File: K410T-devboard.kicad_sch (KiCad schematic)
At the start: 0 parts

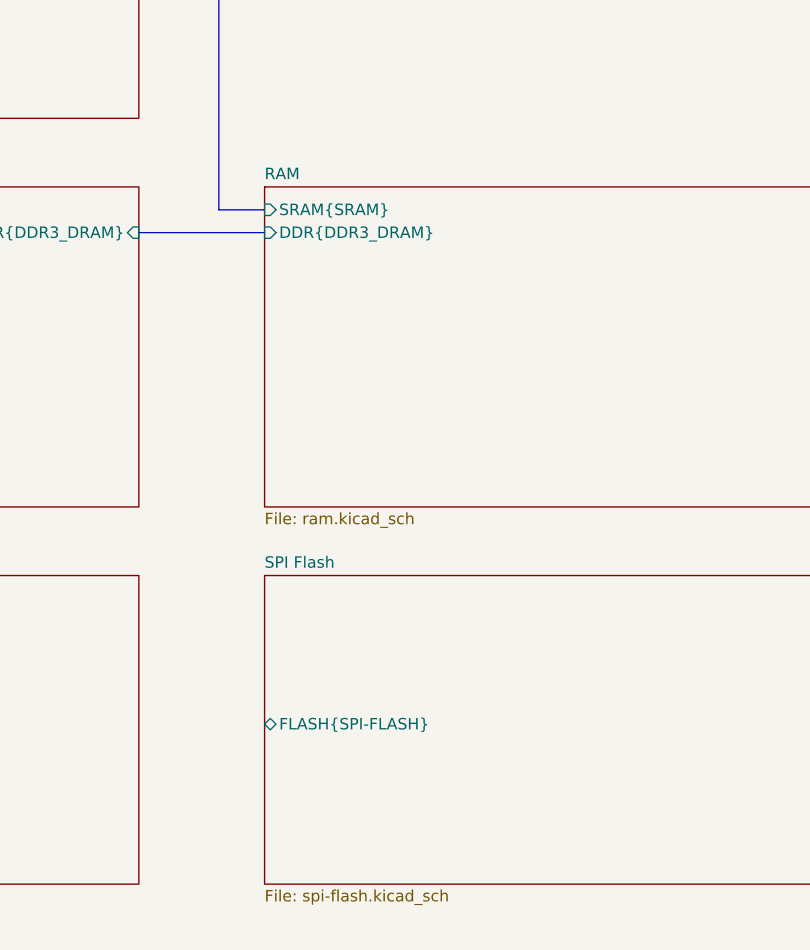
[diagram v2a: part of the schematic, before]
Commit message: Add SD-CARD bus. Add user SPI flash, rename main SPI flash bus. Add uSD card slot
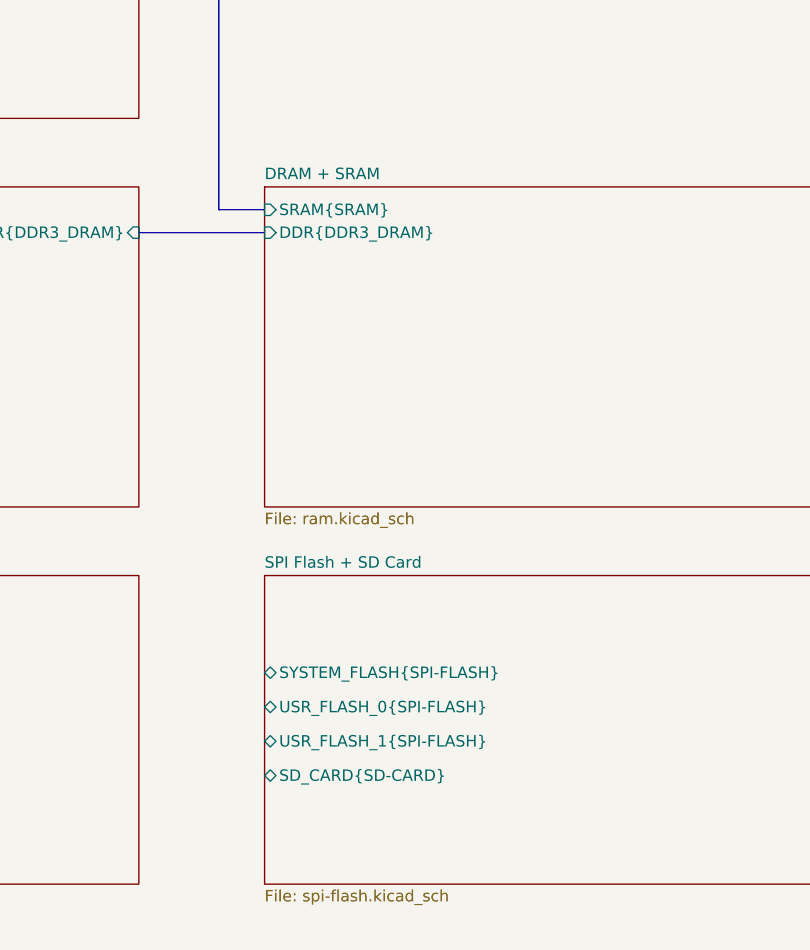
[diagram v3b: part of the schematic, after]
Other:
- sheet RAM renamed DRAM + SRAM
- sheet SPI Flash renamed SPI Flash + SD Card
- sheet SPI Flash + SD Card ports: added SD_CARD{SD-CARD}, SYSTEM_FLASH{SPI-FLASH}, USR_FLASH_0{SPI-FLASH}, USR_FLASH_1{SPI-FLASH}; removed FLASH{SPI-FLASH}

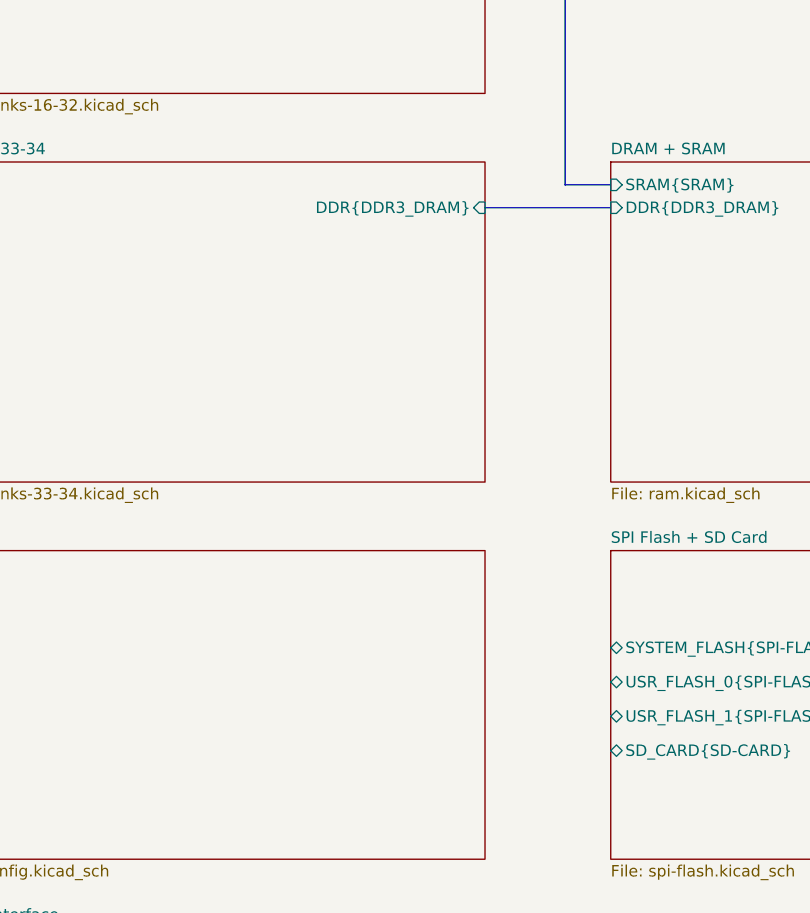
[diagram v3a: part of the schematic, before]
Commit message: Connect SD_CARD and USR_FLASH_0 to FPGA
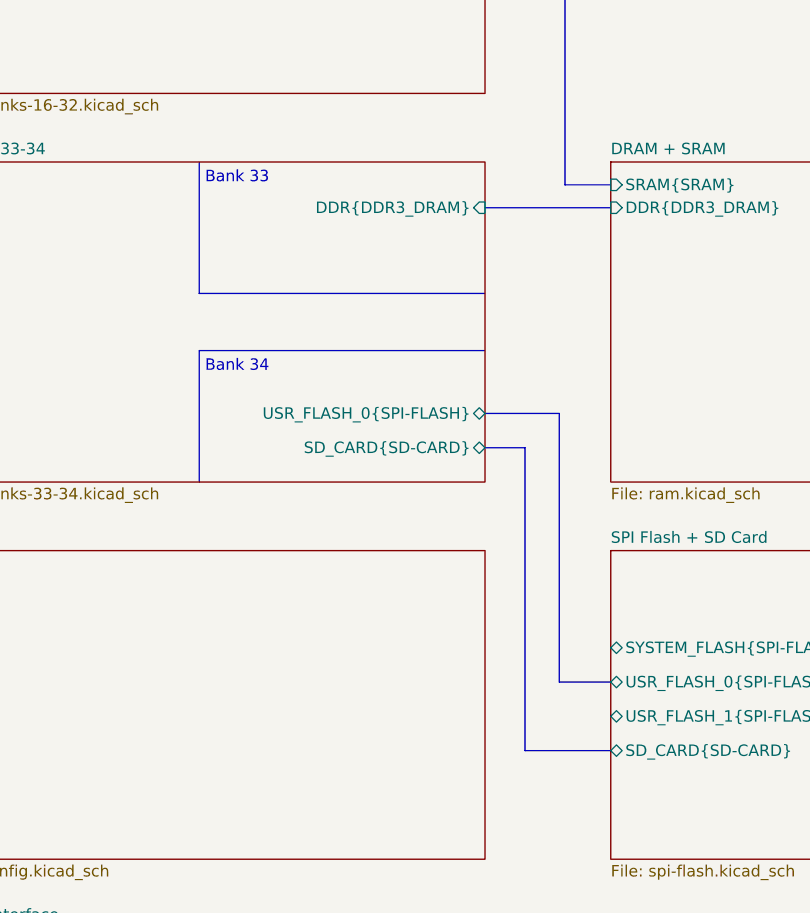
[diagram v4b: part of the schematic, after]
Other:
- sheet FPGA banks 33-34 ports: added SD_CARD{SD-CARD}, USR_FLASH_0{SPI-FLASH}; removed none
- note added: "Bank 33"
- note added: "Bank 34"
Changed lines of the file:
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@@
     (rev "0.0.99")
   )
+  (bus_alias "SRAM" (members "A[0..19]" "DQ[0..7]" "CE2" "~{CE}" "~{WE}" "~{OE}"))
+  (bus_alias "DDR3_DRAM" (members "A[0..15]" "BA[0..2]" "DQ[0..7]" "DQS_P" "DQS_N" "TDQS_P" "TDQS_N" "~{WE}" "~{CAS}" "~{RAS}" "~{CS}" "CKE" "CK_N" "CK_P" "ODT" "~{RESET}" "DM"))
+  (bus_alias "SD-CARD" (members "DAT[0..3]" "~{CD}" "CLK" "CMD"))
+  (bus_alias "SPI-FLASH" (members "~{CS}" "DQ[0..3]" "~{WP}" "~{HOLD}" "CLK"))
   (bus_alias "JTAG" (members "TMS" "TCK" "TDI" "TDO"))
-  (bus_alias "SPI-FLASH" (members "~{CS}" "DQ[0..3]" "~{WP}" "~{HOLD}" "CLK"))
-  (bus_alias "SD-CARD" (members "DAT[0..3]" "~{CD}" "CLK" "CMD"))
-  (bus_alias "DDR3_DRAM" (members "A[0..15]" "BA[0..2]" "DQ[0..7]" "DQS_P" "DQS_N" "TDQS_P" "TDQS_N" "~{WE}" "~{CAS}" "~{RAS}" "~{CS}" "CKE" "CK_N" "CK_P" "ODT" "~{RESET}" "DM"))
-  (bus_alias "SRAM" (members "A[0..19]" "DQ[0..7]" "CE2" "~{CE}" "~{WE}" "~{OE}"))
+  (bus (pts (xy 252.095 170.815) (xy 261.62 170.815))
+    (stroke (width 0) (type default) (color 0 0 0 0))
+  )
+  (polyline (pts (xy 215.9 120.015) (xy 247.65 120.015))
+    (stroke (width 0) (type solid) (color 0 0 0 0))
+  )
+  (bus (pts (xy 247.65 137.16) (xy 252.095 137.16))
+    (stroke (width 0) (type default) (color 0 0 0 0))
+  )
+  (bus (pts (xy 255.905 163.195) (xy 261.62 163.195))
+    (stroke (width 0) (type default) (color 0 0 0 0))
+  )
   (bus (pts (xy 256.54 107.95) (xy 256.54 21.59))
     (stroke (width 0) (type default) (color 0 0 0 0))
   )
   (bus (pts (xy 261.62 107.95) (xy 256.54 107.95))
+    (stroke (width 0) (type default) (color 0 0 0 0))
+  )
+  (bus (pts (xy 255.905 133.35) (xy 255.905 163.195))
+    (stroke (width 0) (type default) (color 0 0 0 0))
+  )
+  (polyline (pts (xy 215.9 126.365) (xy 247.65 126.365))
+    (stroke (width 0) (type solid) (color 0 0 0 0))
+  )
+  (bus (pts (xy 252.095 137.16) (xy 252.095 170.815))
     (stroke (width 0) (type default) (color 0 0 0 0))
   )
@@
   (bus (pts (xy 247.65 110.49) (xy 261.62 110.49))
     (stroke (width 0) (type default) (color 0 0 0 0))
+  )
+  (polyline (pts (xy 215.9 120.015) (xy 215.9 105.41))
+    (stroke (width 0) (type solid) (color 0 0 0 0))
+  )
+  (bus (pts (xy 247.65 133.35) (xy 255.905 133.35))
+    (stroke (width 0) (type default) (color 0 0 0 0))
+  )
+  (polyline (pts (xy 215.9 140.97) (xy 215.9 126.365))
+    (stroke (width 0) (type solid) (color 0 0 0 0))
+  )
+  (text "Bank 34" (at 216.535 128.905 0)
+    (effects (font (size 1.27 1.27)) (justify left bottom))
+  )
+  (text "Bank 33" (at 216.535 107.95 0)
+    (effects (font (size 1.27 1.27)) (justify left bottom))
   )
   (sheet (at 182.88 237.49) (size 64.77 34.29) (fields_autoplaced)
@@
       (effects (font (size 1.27 1.27)) (justify right))
     )
+    (pin "USR_FLASH_0{SPI-FLASH}" bidirectional (at 247.65 133.35 0)
+      (effects (font (size 1.27 1.27)) (justify right))
+    )
+    (pin "SD_CARD{SD-CARD}" bidirectional (at 247.65 137.16 0)
+      (effects (font (size 1.27 1.27)) (justify right))
+    )

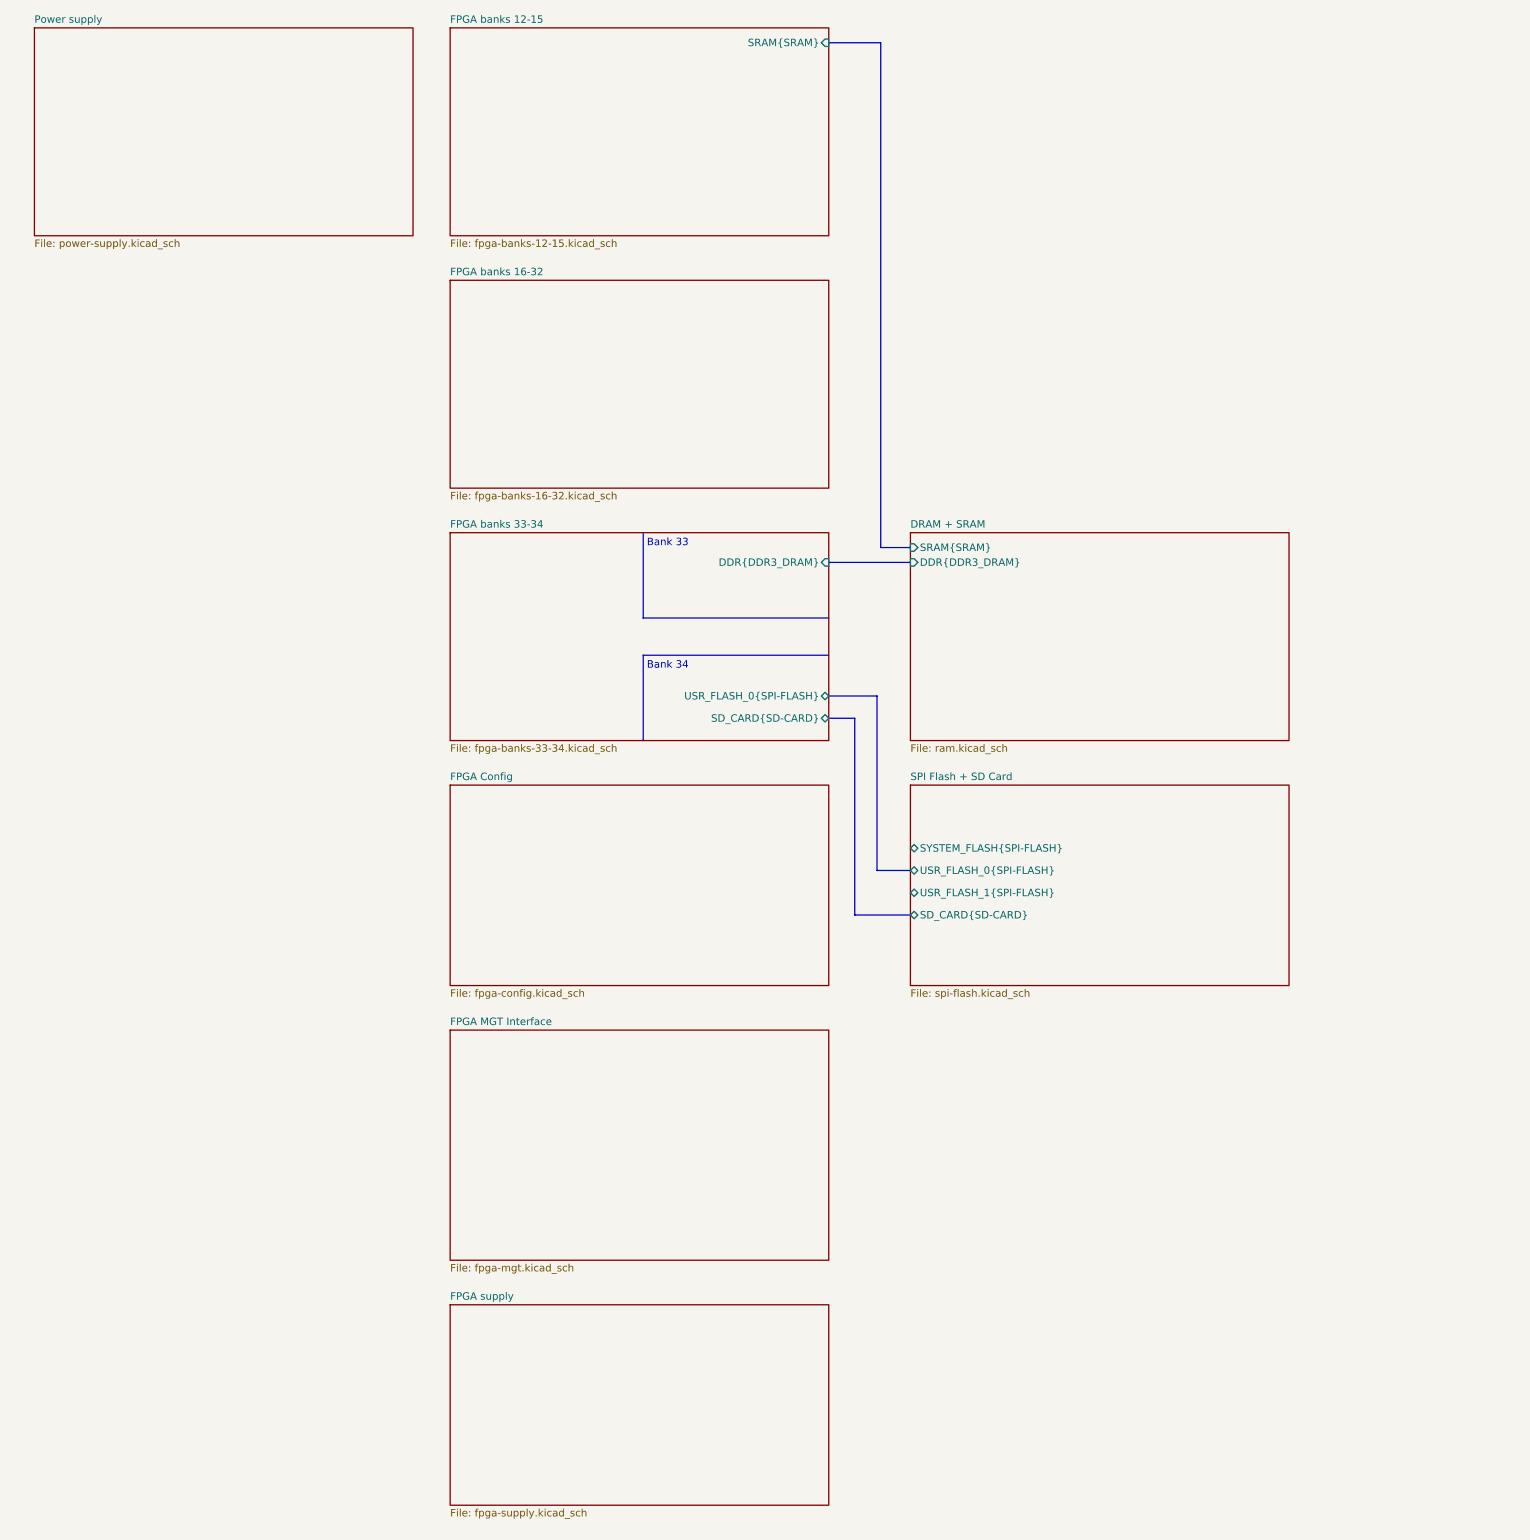
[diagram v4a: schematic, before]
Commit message: Update system SPI Flash bus name, rearrange sheets
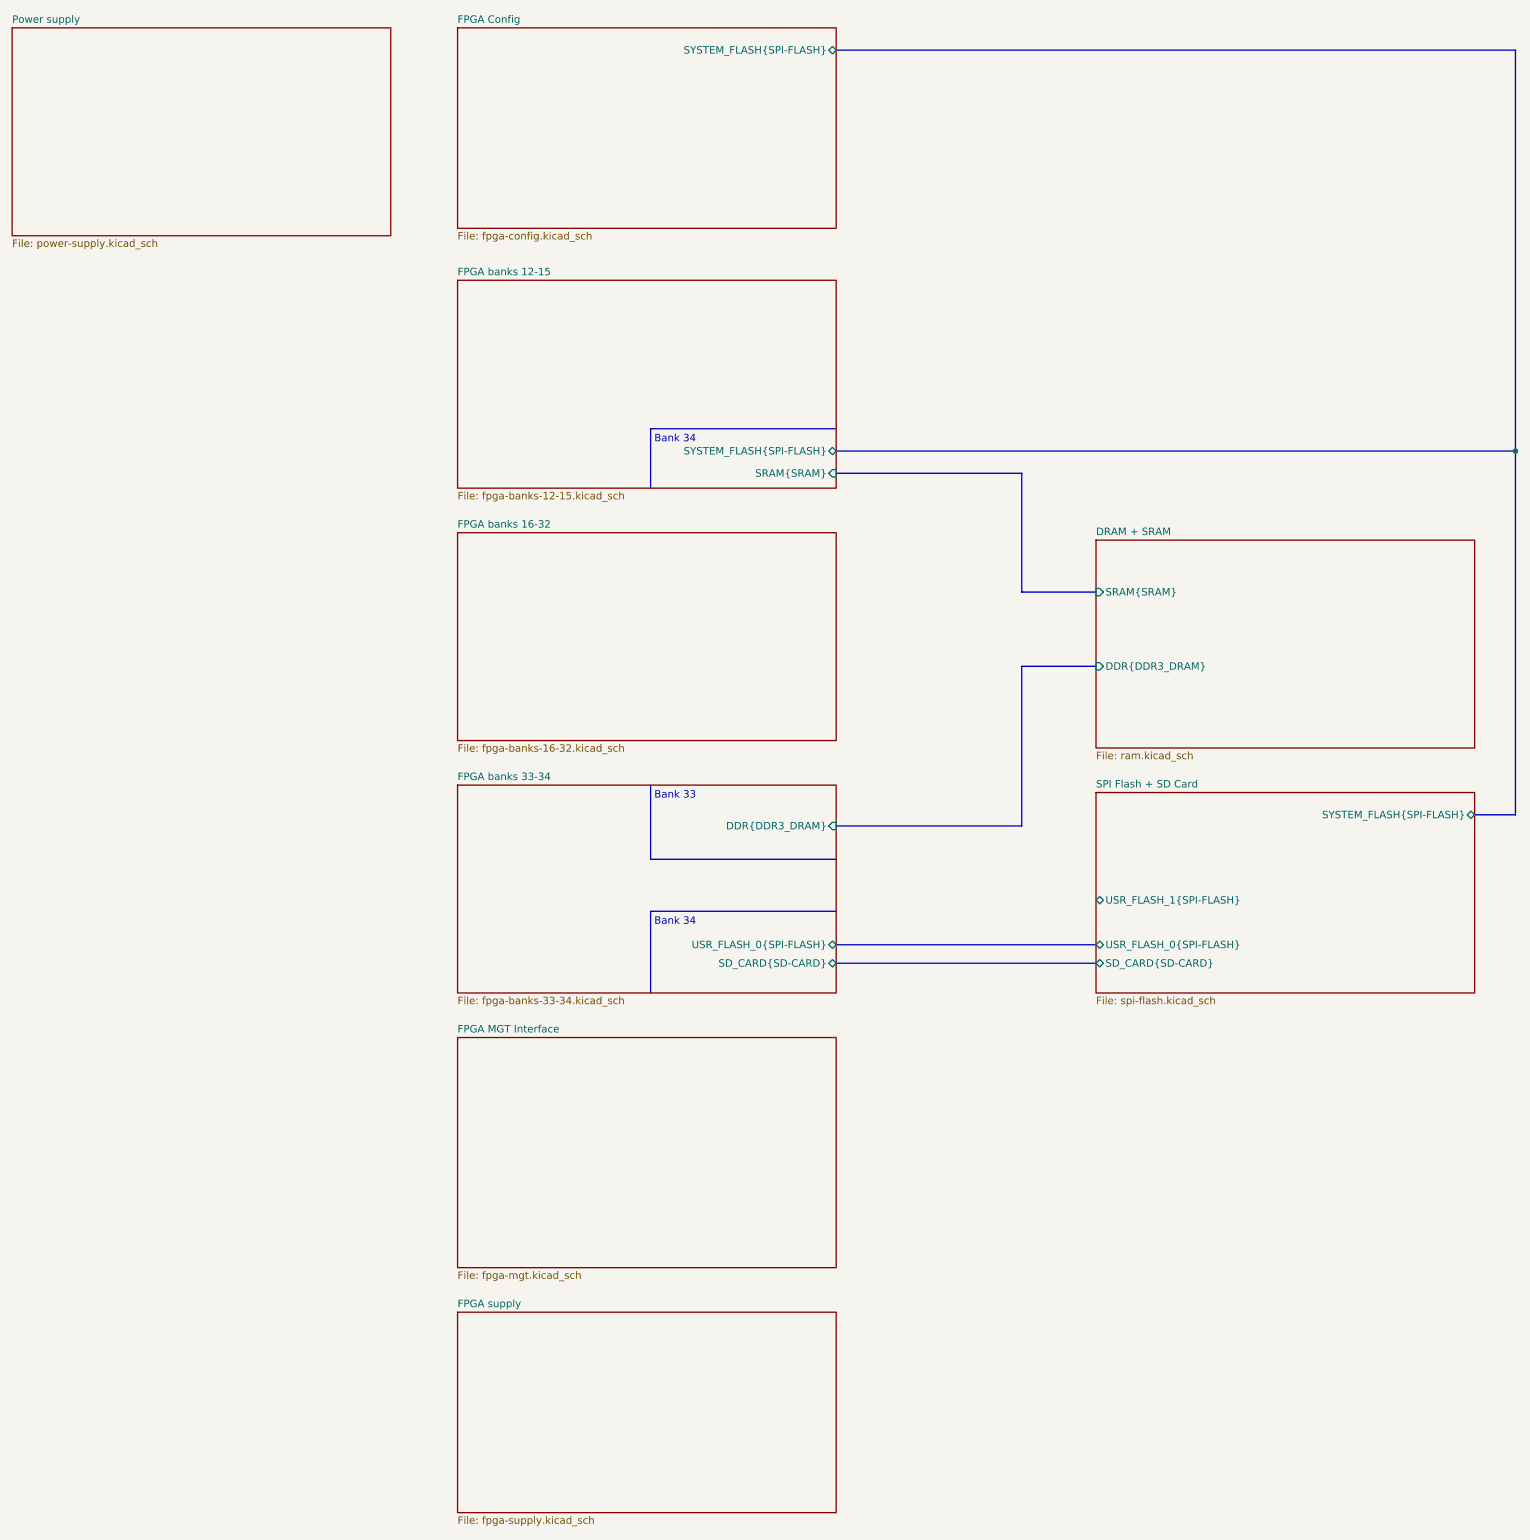
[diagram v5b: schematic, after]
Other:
- sheet FPGA Config ports: added SYSTEM_FLASH{SPI-FLASH}; removed none
- sheet FPGA banks 12-15 ports: added SYSTEM_FLASH{SPI-FLASH}; removed none

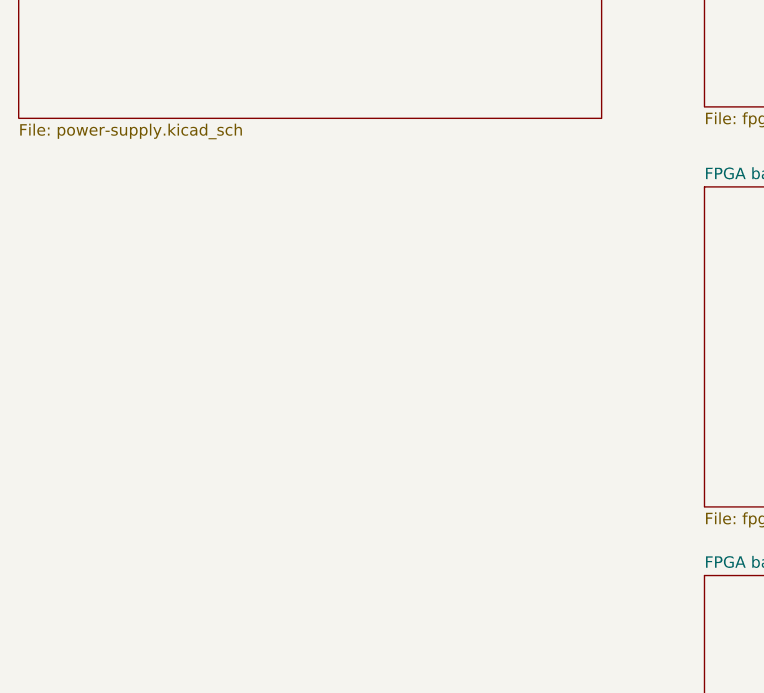
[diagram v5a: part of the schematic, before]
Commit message: Unify sheets tables, add user-gpio sheet
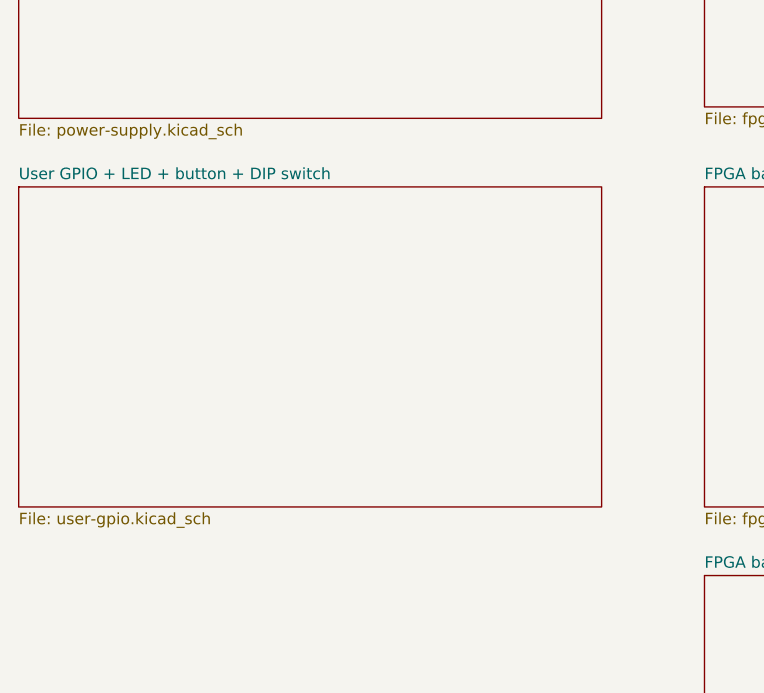
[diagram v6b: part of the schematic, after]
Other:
- added sheet User GPIO + LED + button + DIP switch (user-gpio.kicad_sch)
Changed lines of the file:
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@@
+    )
+  )
+  (sheet (at 107.95 62.23) (size 64.77 35.56) (fields_autoplaced)
+    (stroke (width 0.1524) (type solid) (color 0 0 0 0))
+    (fill (color 0 0 0 0.0000))
+    (property "Sheet name" "User GPIO + LED + button + DIP switch" (id 0) (at 107.95 61.5184 0)
+      (effects (font (size 1.27 1.27)) (justify left bottom))
+    )
+    (property "Sheet file" "user-gpio.kicad_sch" (id 1) (at 107.95 98.3746 0)
+      (effects (font (size 1.27 1.27)) (justify left top))
     )
   )
@@
     (path "/f197fc77-508c-435d-932d-162b52b3ed75" (page "9"))
     (path "/53e5e9d0-da1a-4e72-8926-4916ab1fc9d9" (page "10"))
+    (path "/92f84d48-430a-4861-a72f-ac293d5b94b2" (page "11"))
   )
   (symbol_instances
